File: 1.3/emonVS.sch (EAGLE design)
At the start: 46 parts, among them CN1 TERMINAL_BLOCK_5P, CN2 RJ45 Jack, CN3 TERMINAL_BLOCK_2P, T1 ZMPT101B, T2 ZMPT101B, T3 ZMPT101B

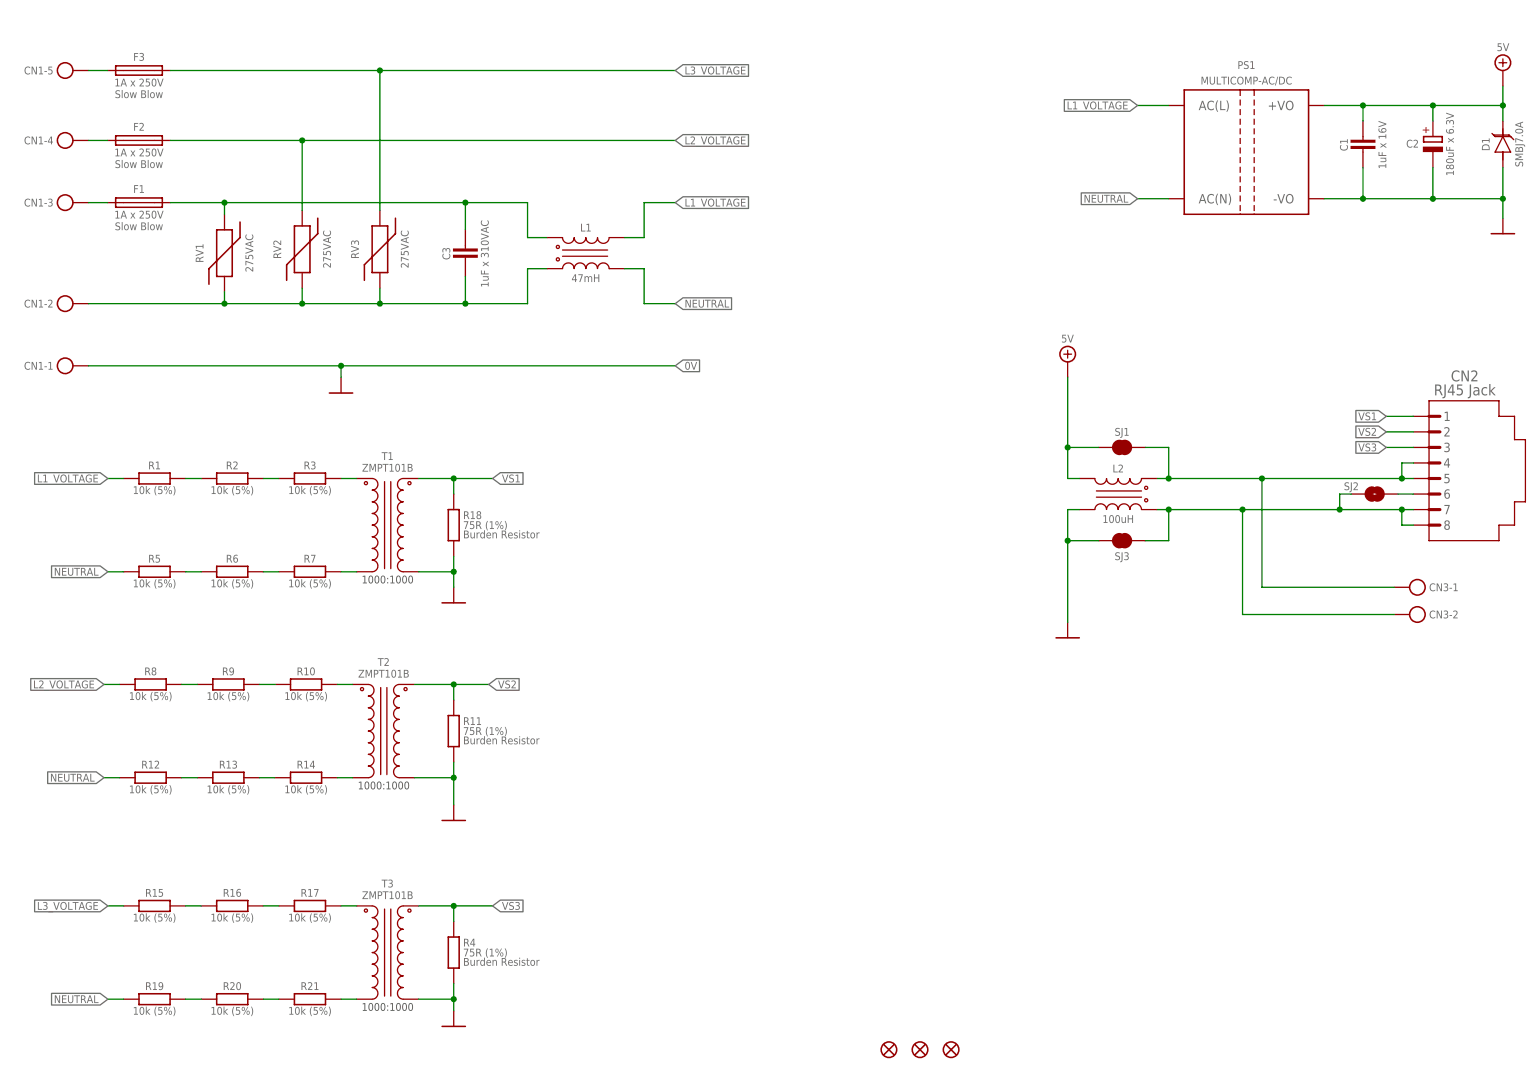
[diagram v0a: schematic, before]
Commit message: added note about the L2 choke use
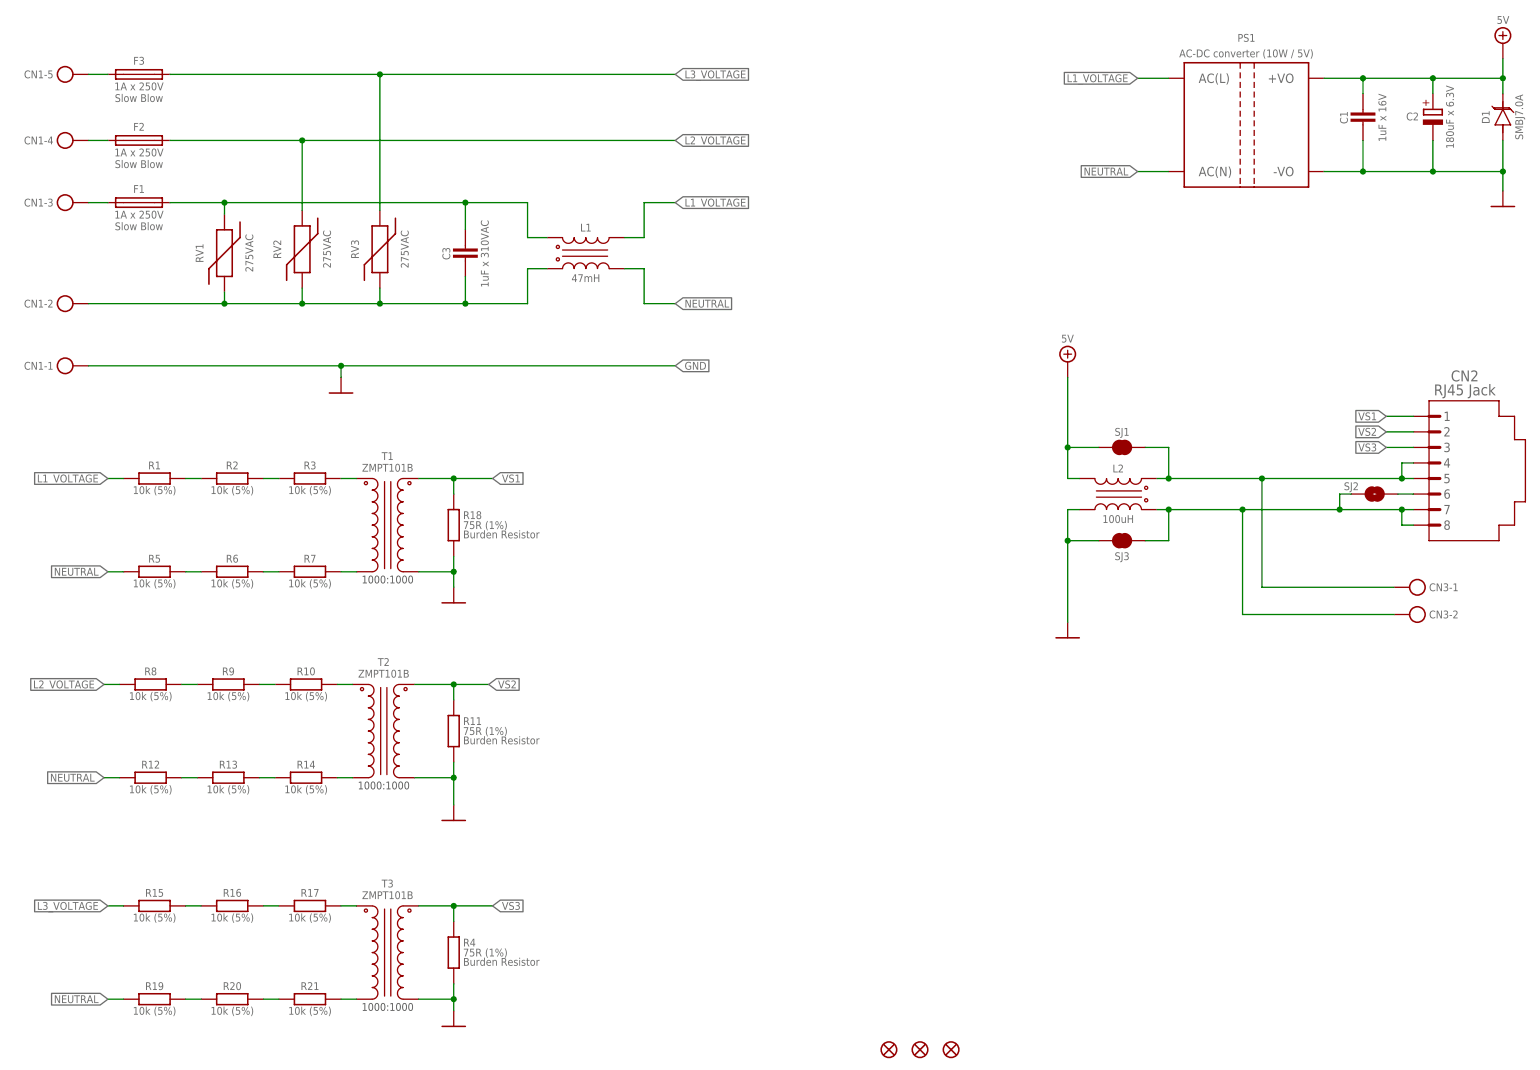
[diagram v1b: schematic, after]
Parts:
- PS1: value MULTICOMP-AC/DC -> AC-DC converter (10W / 5V); PN MP-LD05-23B05R2 -> MP-LD10-23B05R2
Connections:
- net 0V renamed GND
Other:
- note added: "by default L2 = DNP in order to use the choke, cut the trace between pads of the SJ1 and SJ3."
- moved on the sheet: C1, C2, CN1-5, D1, F3, PS1

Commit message: Renumbered resistor designators to be backwards compatible with older versions
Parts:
- removed R10, R13, R14, R7: 10k (5%), My-RLC:R_0603
- removed R11: 75R (1%), OpenEnergyMonitor:R_
- added R25, R27, R28, R29, R30: 10k (5%), My-RLC:R_0603
- R18, R4: value 75R (1%) -> 10k (5%); device OpenEnergyMonitor:R_ -> My-RLC:R_0603; PN ERJ-H3EF75R0V -> ERJ-H3GJ103V
- R21, R8, R9: value 10k (5%) -> 75R (1%); device My-RLC:R_0603 -> OpenEnergyMonitor:R_; PN ERJ-H3GJ103V -> ERJ-H3EF75R0V
- renumbered R20 to R26
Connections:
- net GND: now also R21.2, R8.2, R9.2; no longer R11.2, R18.2, R4.2
- net L1_VOLTAGE: now also R6.2; no longer R1.2
- net L2_VOLTAGE: now also R19.2; no longer R8.2
- net L3_VOLTAGE: now also R30.2; no longer R15.2
- net N$1: now also R4.1; no longer R3.1
- net N$10: now also R17.1; no longer R10.1
- net N$11: now also R12.1; no longer R14.1
- net N$12: now also R12.2, R15.1; no longer R13.1, R14.2
- net N$13: now also R17.2, R18.1; no longer R10.2, R9.1
- net N$14: now also R18.2, R19.1; no longer R8.1, R9.2
- net N$15: now also R15.2, R16.1; no longer R12.1, R13.2
- net N$18: now also R28.1; no longer R17.1
- net N$19: now also R25.1; no longer R21.1
- net N$2: now also R1.1; no longer R7.1
- net N$21: now also R25.2; no longer R21.2
- net N$22: now also R28.2, R29.1; no longer R16.1, R17.2
- net N$23: now also R29.2, R30.1; no longer R15.1, R16.2
- net N$24: now also R27.1; no longer R19.1
- net N$3: now also R1.2, R2.1; no longer R6.1, R7.2
- net N$4: now also R4.2, R5.1; no longer R2.1, R3.2
- net N$5: now also R5.2, R6.1; no longer R1.1, R2.2
- net N$6: now also R2.2, R3.1; no longer R5.1, R6.2
- net NEUTRAL: now also R16.2, R27.2, R3.2; no longer R12.2, R19.2, R5.2
- net VS1: now also R9.1; no longer R18.1
- net VS2: now also R8.1; no longer R11.1
- net VS3: now also R21.1; no longer R4.1
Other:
- moved on the sheet: R1, R12, R15, R16, R17, R18, R19, R2, R21, R3, R4, R5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
